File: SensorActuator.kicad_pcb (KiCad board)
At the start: 2 copper layers, 50 x 38 mm, 32 parts, among them IC1 STM32L051K8T6, P1 CONN_02X06, P3 CONN_02X04, P4 CONN_01X04, P5 CONN_01X02, Q1 PMosfetGen, Q2 PMosfetGen, Q4 PMosfetGen, Q5 AO3401, SW1 SW_PUSH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

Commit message: Correct some schematics and add todos on pcb
Signed-off-by: Philip Luyckx <philip.luyckx@gmail.com>
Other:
- board text added: "Check footprint mosfets Check footprint inductor (it seems the pads are to small under the component) Add holes for lens"
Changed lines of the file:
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@@
-(kicad_pcb (version 4) (host pcbnew 4.0.0-2.201512091501+6195~38~ubuntu15.10.1-stable)
+(kicad_pcb (version 4) (host pcbnew 4.0.1-3.201512221401+6198~38~ubuntu15.10.1-stable)
   (general
     (links 85)
@@
     (area 76.771667 51.15 139.8 103.825001)
     (thickness 1.6)
-    (drawings 9)
+    (drawings 10)
     (tracks 355)
     (zones 0)
@@
     )
   )
+  (gr_text "Check footprint mosfets\nCheck footprint inductor (it seems the pads are to small under the component)\nAdd holes for lens" (at 138.1 53.1) (layer Cmts.User)
+    (effects (font (size 1.5 1.5) (thickness 0.3)) (justify left))
+  )
   (target plus (at 124 69) (size 2) (width 0.15) (layer Edge.Cuts))

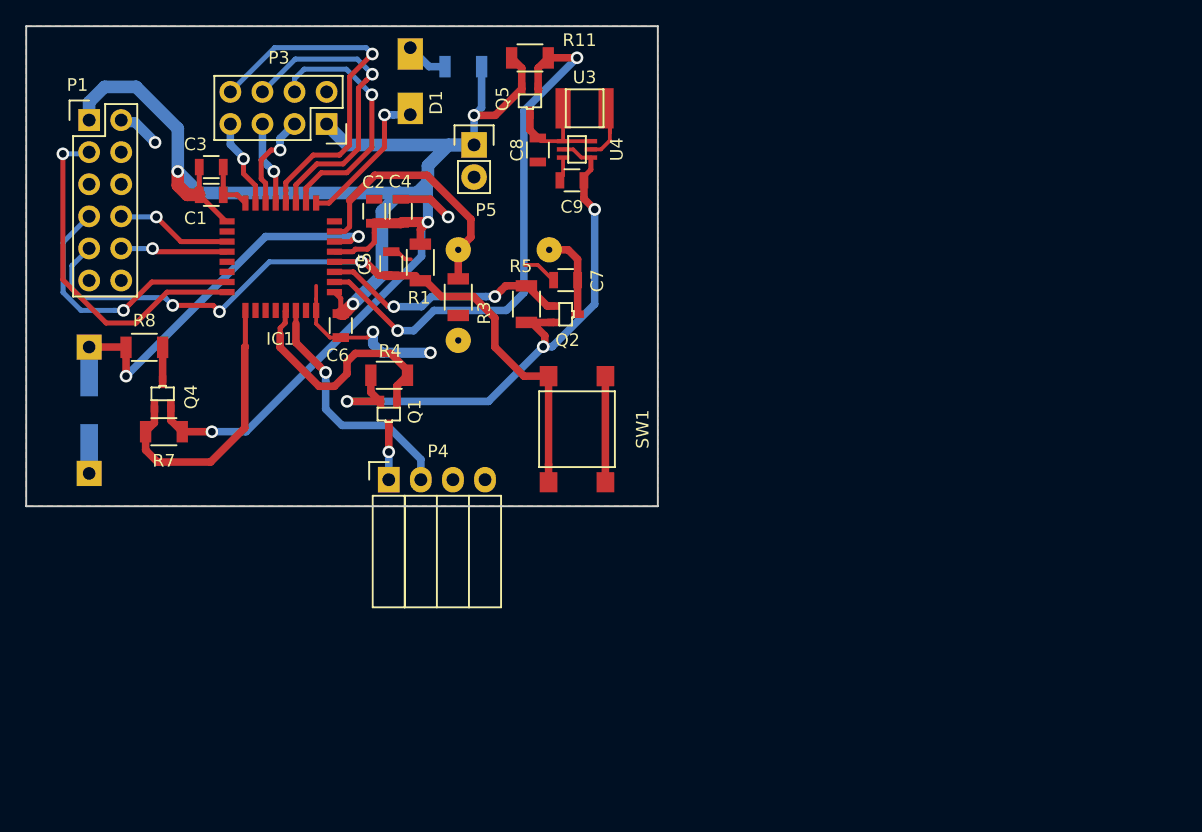
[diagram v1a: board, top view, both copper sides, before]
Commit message: Update schematic and reroute print
 * Update opamp circuit for light sensor
 * Change opamp
 * Reroute everything

Signed-off-by: Philip Luyckx <philip.luyckx@gmail.com>
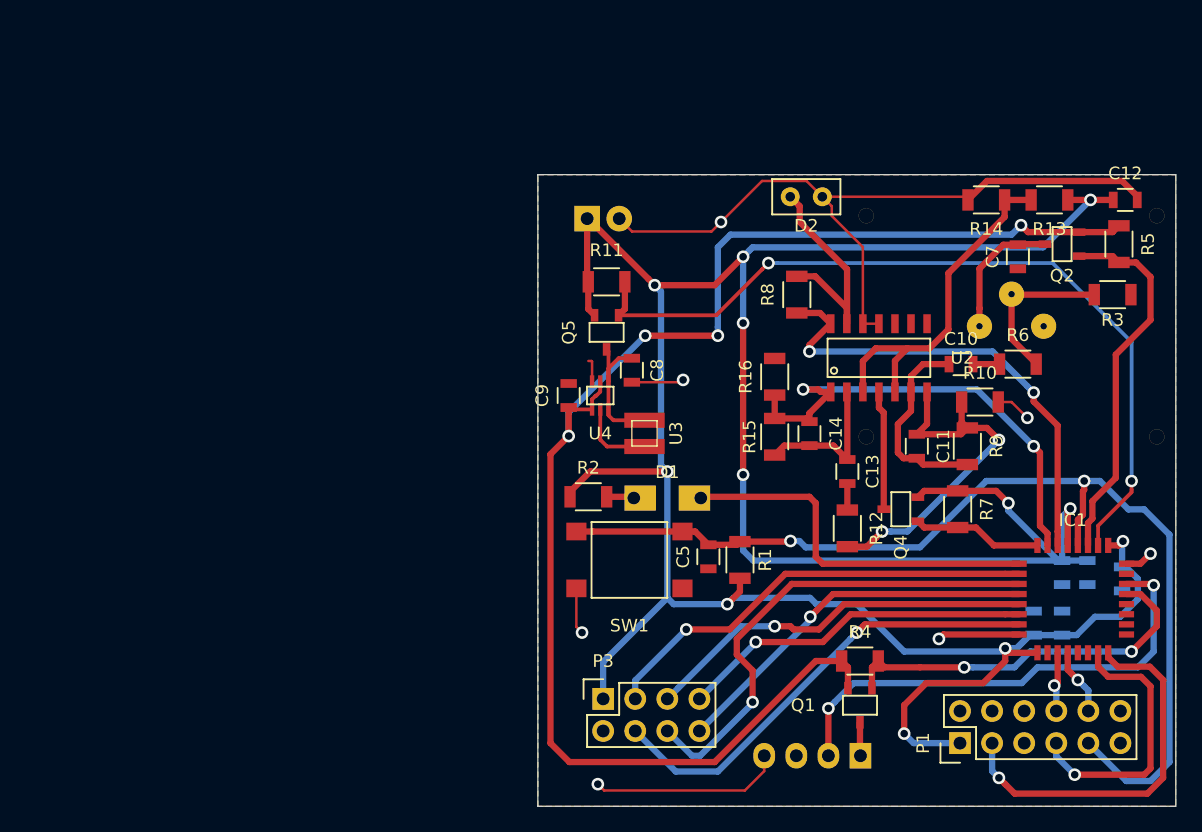
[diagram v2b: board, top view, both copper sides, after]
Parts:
- added C10: 10uF, Resistors_SMD:R_0805, F.Cu at (151.0, 83.8)
- added C11: 100nF, Resistors_SMD:R_0805, F.Cu at (147.5, 90.2)
- added C12: C, Resistors_SMD:R_0805, F.Cu at (164.0, 70.8)
- added C13: 10uF, Resistors_SMD:R_0805, F.Cu at (142.0, 92.2)
- added C14: 100nF, Resistors_SMD:R_0805, F.Cu at (139.0, 89.2)
- added D2: PhotoDiode, CustomModules:PD638C, F.Cu at (138.8, 70.5)
- added R10: 10k, Resistors_SMD:R_1206, F.Cu at (152.5, 86.8)
- added R12: 10k, Resistors_SMD:R_1206, F.Cu at (142.0, 96.8)
- added R13: R, Resistors_SMD:R_1206, F.Cu at (158.0, 70.8)
- added R14: R, Resistors_SMD:R_1206, F.Cu at (153.0, 70.8)
- added R15: 1M, Resistors_SMD:R_1206, F.Cu at (136.2, 89.5)
- added R16: 10k, Resistors_SMD:R_1206, F.Cu at (136.2, 84.8)
- added R6: 10k, Resistors_SMD:R_1206, F.Cu at (155.5, 83.8)
- added U2: MCP6004, CustomSmd:SOIC-14, F.Cu at (144.5, 83.2)
- C1, C2, C3, C4, C6, P4, P5: moved to B.Cu
- Q1, Q2, Q4, Q5: footprint SMD_Packages:SOT-323 -> CustomSmd:SOT23
- R2: moved to F.Cu
- R3: value R -> 100k
- R8: value R -> 3600
- R9: value Photores -> 1M; footprint Resistors_Universal:Resistor_SMD+THTuniversal_1206_RM10_HandSoldering -> Resistors_SMD:R_1206; moved to F.Cu
- moved P1 84.8 mm to (150.9, 113.8), turned to 90 degrees
- moved C1 75.4 mm to (159.0, 104.2), turned to 90 degrees
- moved C3 74.4 mm to (156.8, 104.2), turned to 90 degrees
- moved R9 69.6 mm to (151.5, 90.2)
- moved IC1 68.3 mm to (159.8, 102.3), turned to 180 degrees
- moved C6 65.0 mm to (163.8, 100.8)
- moved R7 63.1 mm to (150.7, 95.2), turned to 270 degrees
- moved C2 61.5 mm to (159.0, 100.2), turned to 270 degrees
- moved C4 61.4 mm to (161.0, 100.2), turned to 270 degrees
- moved Q4 59.1 mm to (146.2, 95.2), turned to 90 degrees
- moved R8 51.8 mm to (138.0, 78.2), turned to 90 degrees
- moved R3 51.8 mm to (163.0, 78.2), turned to 0 degrees
- moved P3 50.5 mm to (122.7, 110.2), turned to 0 degrees
- moved R5 47.1 mm to (163.5, 74.2), turned to 270 degrees
- moved Q1 43.8 mm to (143.0, 110.8), turned to 180 degrees
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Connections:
- IC1 pad 10: RF_CE -> RF_CSN
- IC1 pad 14: RF_CSN -> RF_IRQ
- IC1 pad 15: RF_IRQ -> RF_CE
- IC1 pad 18: Net-(IC1-Pad18) -> (no net)
- IC1 pad 21: Net-(IC1-Pad21) -> (no net)
- IC1 pad 22: Net-(IC1-Pad22) -> (no net)
- IC1 pad 25: LightSensEnable -> (no net)
- IC1 pad 26: Net-(IC1-Pad26) -> (no net)
- IC1 pad 27: Net-(IC1-Pad27) -> (no net)
- IC1 pad 28: Net-(IC1-Pad28) -> (no net)
- IC1 pad 31: Net-(IC1-Pad31) -> (no net)
- IC1 pad 8: Net-(IC1-Pad8) -> LightSensEnable
- P1 pad 11: Net-(P1-Pad11) -> (no net)
- P1 pad 12: Net-(P1-Pad12) -> (no net)
- P1 pad 4: Net-(P1-Pad4) -> (no net)
- P1 pad 6: Net-(P1-Pad6) -> (no net)
- Q4 pad 3: Net-(Q4-Pad3) -> Opamp_V+
- R3 pad 1: ADC_Motion -> Motion_Out
- R8 pad 1: Net-(Q4-Pad3) -> ADC_Light
- R8 pad 2: ADC_Light -> Net-(D2-Pad1)
- R9 pad 1: ADC_Light -> Net-(C11-Pad1)
- R9 pad 2: GND -> Net-(C10-Pad2)
- U1 pad 2: ADC_Motion -> Motion_Out
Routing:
- net +BATT: track 133.4 -> 245.6 mm, vias 5 -> 12
- net +5V: track 47.5 -> 117.3 mm, vias 3 -> 4
- net GND: track 45.0 -> 95.1 mm, vias 4 -> 7
- net Net-(C11-Pad1): track 0.00 -> 29.0 mm, vias 0 -> 2
- net Motion_Offset: track 0.00 -> 28.3 mm
- net RF_CSN: track 7.91 -> 35.3 mm
- net SPI_RF_MOSI: track 6.99 -> 31.2 mm
- net MCU_RST: track 59.7 -> 83.3 mm, vias 3 -> 2
- net Enable5V: track 43.3 -> 65.0 mm
- net RF_IRQ: track 7.08 -> 28.1 mm
- net Temp_1Wire: track 19.6 -> 38.8 mm, vias 1 -> 2
- net Net-(D2-Pad1): track 0.00 -> 18.2 mm
- net MCU_LED: track 11.9 -> 29.9 mm, vias 1 -> 0
- net ADC_Motion: track 20.4 -> 38.4 mm, vias 0 -> 2
- net RF_CE: track 20.2 -> 36.5 mm
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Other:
- board size 50 x 38 mm -> 50.5 x 50 mm
- net class BoostConv added: clearance 0.2, trace_width 0.3, via_dia 1, via_drill 0.6
- net class Default: clearance 0.3 -> 0.25; trace_width 0.3 -> 0.5
- net class GND added: clearance 0.2, trace_width 0.2, via_dia 1, via_drill 0.6
- net class Opamp added: clearance 0.25, trace_width 0.5, via_dia 1, via_drill 0.6
- net class mcu added: clearance 0.2, trace_width 0.3, via_dia 1, via_drill 0.6
- rule pad_to_mask_clearance: 0.2 -> 0
- rule trace_clearance: 0.3 -> 0.25
- board text removed: "Check footprint mosfets Check footprint inductor (it seems the pads are to small under the component) Add holes for lens"

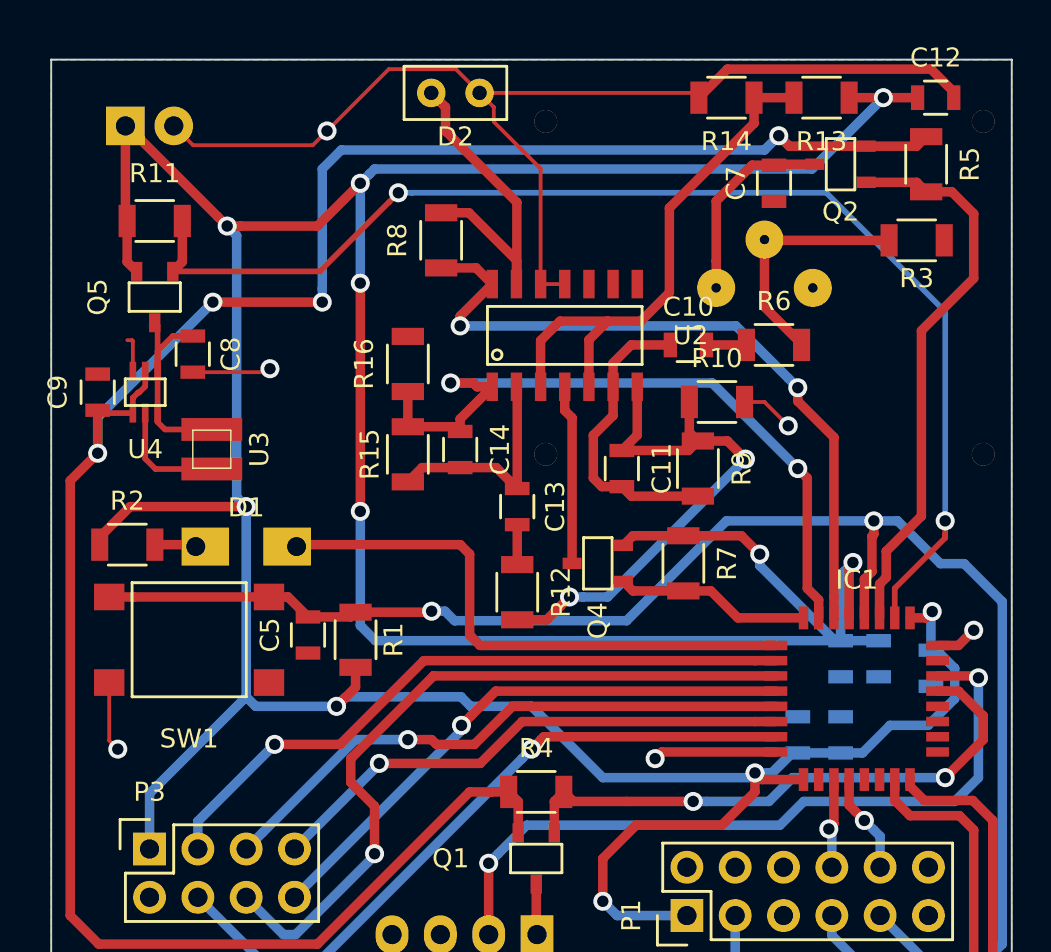
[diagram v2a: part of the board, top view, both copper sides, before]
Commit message: Use 0603 resistors
Signed-off-by: Philip Luyckx <philip.luyckx@gmail.com>
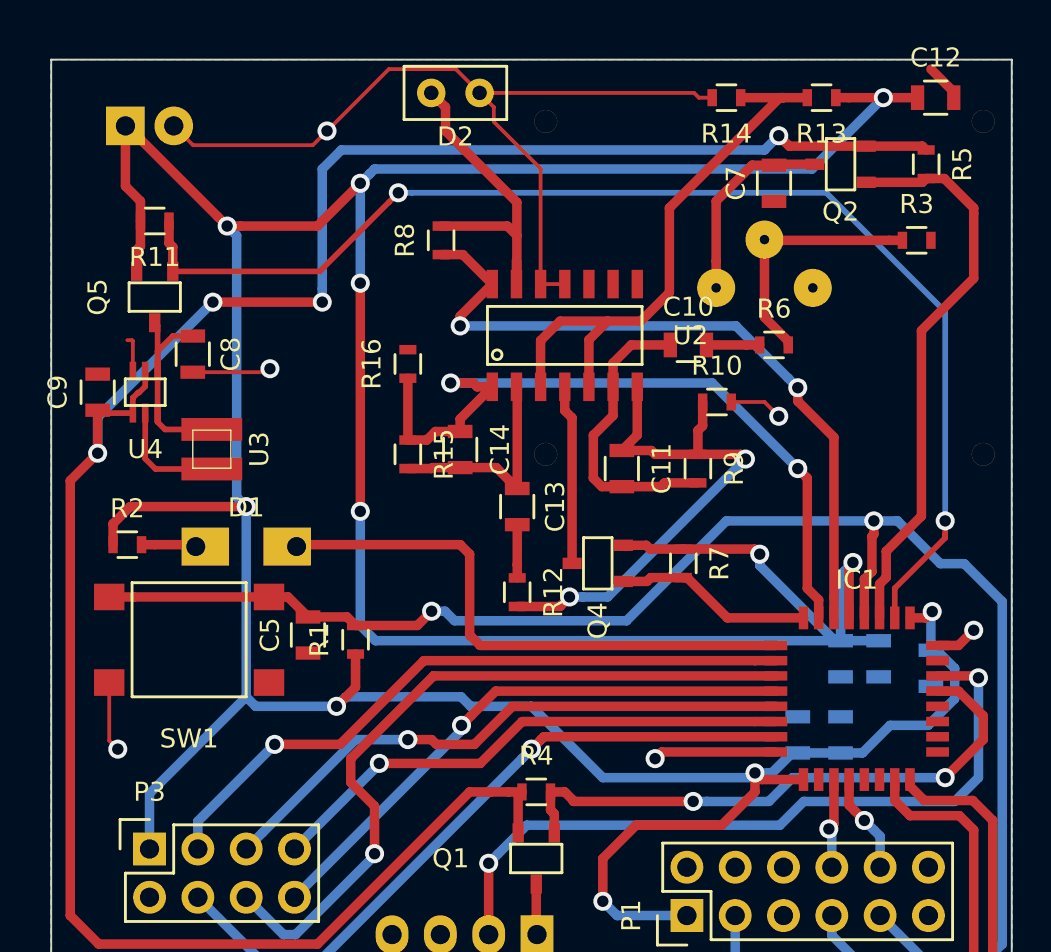
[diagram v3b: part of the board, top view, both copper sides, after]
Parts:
- R1, R13, R14: value R -> 100k; footprint Resistors_SMD:R_1206 -> Resistors_SMD:R_0603
- R10, R11, R12, R15, R16, R3, R6, R8, R9: footprint Resistors_SMD:R_1206 -> Resistors_SMD:R_0603
- R2: value R -> 475; footprint Resistors_SMD:R_1206 -> Resistors_SMD:R_0603
- R4, R5, R7: value R -> 47.5k; footprint Resistors_SMD:R_1206 -> Resistors_SMD:R_0603
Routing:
- net GND: track 95.1 -> 82.9 mm
- net Motion_Offset: track 28.3 -> 30.5 mm
- net ADC_Motion: track 38.4 -> 39.9 mm
- net Net-(D2-Pad1): track 18.2 -> 17.4 mm
- net +BATT: track 245.6 -> 246.4 mm
- net Net-(D1-Pad2): track 2.19 -> 2.89 mm
- net Net-(C13-Pad1): track 2.10 -> 2.80 mm
- net Net-(C10-Pad1): track 2.10 -> 2.80 mm
- net DHT22_Enable: track 30.1 -> 30.8 mm
- net Net-(C11-Pad1): track 29.0 -> 28.4 mm

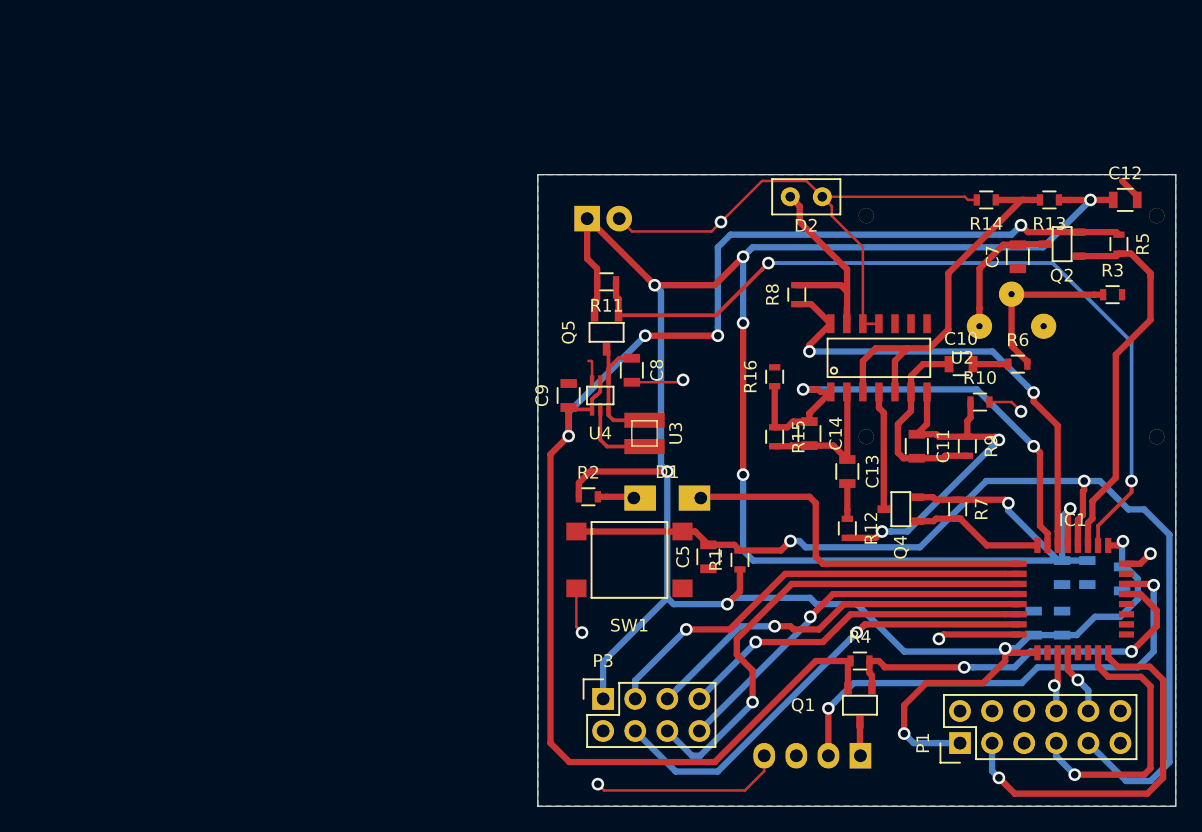
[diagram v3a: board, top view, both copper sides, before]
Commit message: Finalize pcb
 * Make pcb 50x50mm
 * Increase clearance for filled zones

Signed-off-by: Philip Luyckx <philip.luyckx@gmail.com>
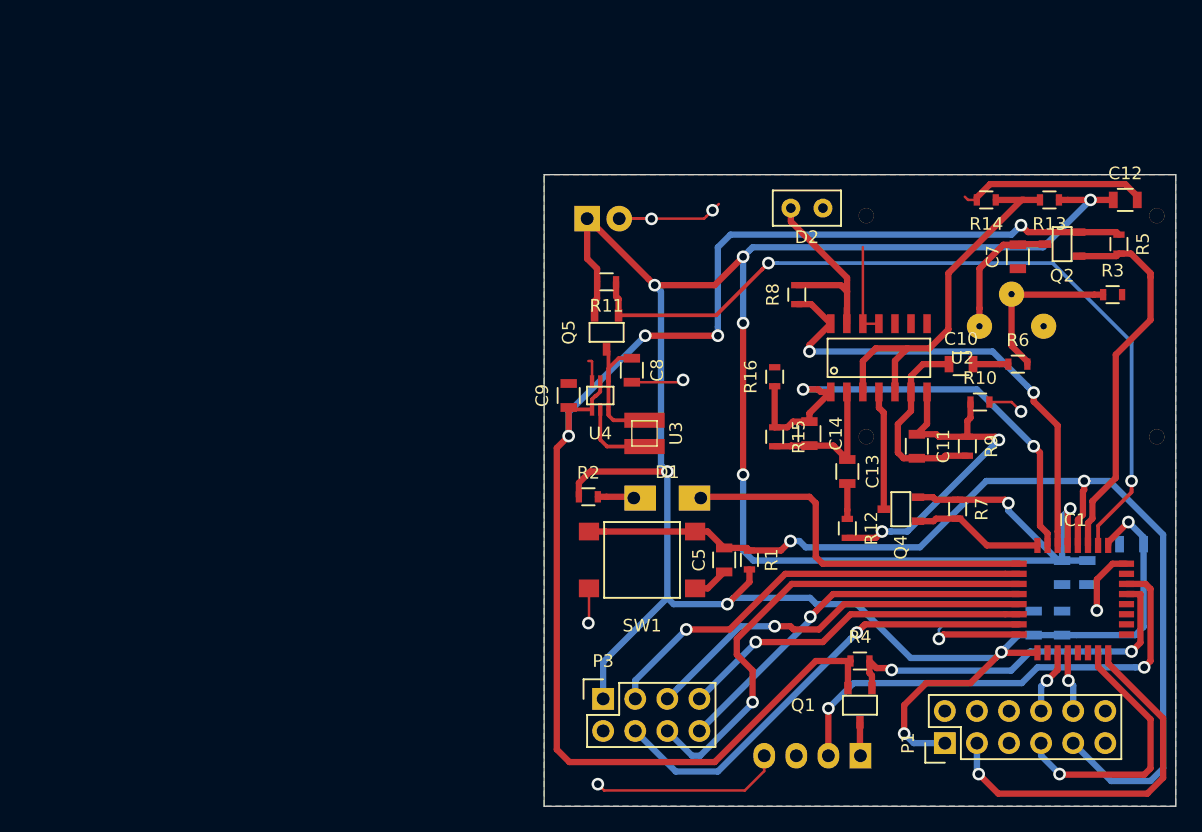
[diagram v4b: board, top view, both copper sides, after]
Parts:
- moved C6 2.85 mm to (164.5, 98.0), turned to 180 degrees
- moved C5 1.27 mm to (132.2, 99.2)
- moved P1 1.20 mm to (149.7, 113.8)
- moved SW1 1.00 mm to (125.8, 99.2)
- moved D2 0.90 mm to (138.8, 71.4)
- moved R1 0.75 mm to (134.2, 99.2)
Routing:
- net GND: track 82.9 -> 76.6 mm, vias 7 -> 8
- net Net-(D2-Pad1): track 17.4 -> 16.4 mm
- net DHT22_Enable: track 30.8 -> 29.9 mm
- net +BATT: track 246.4 -> 247.2 mm
- net MCU_RST: track 83.7 -> 83.2 mm
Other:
- board size 50.5 x 50 mm -> 50 x 50 mm
